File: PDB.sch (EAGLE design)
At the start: 84 parts

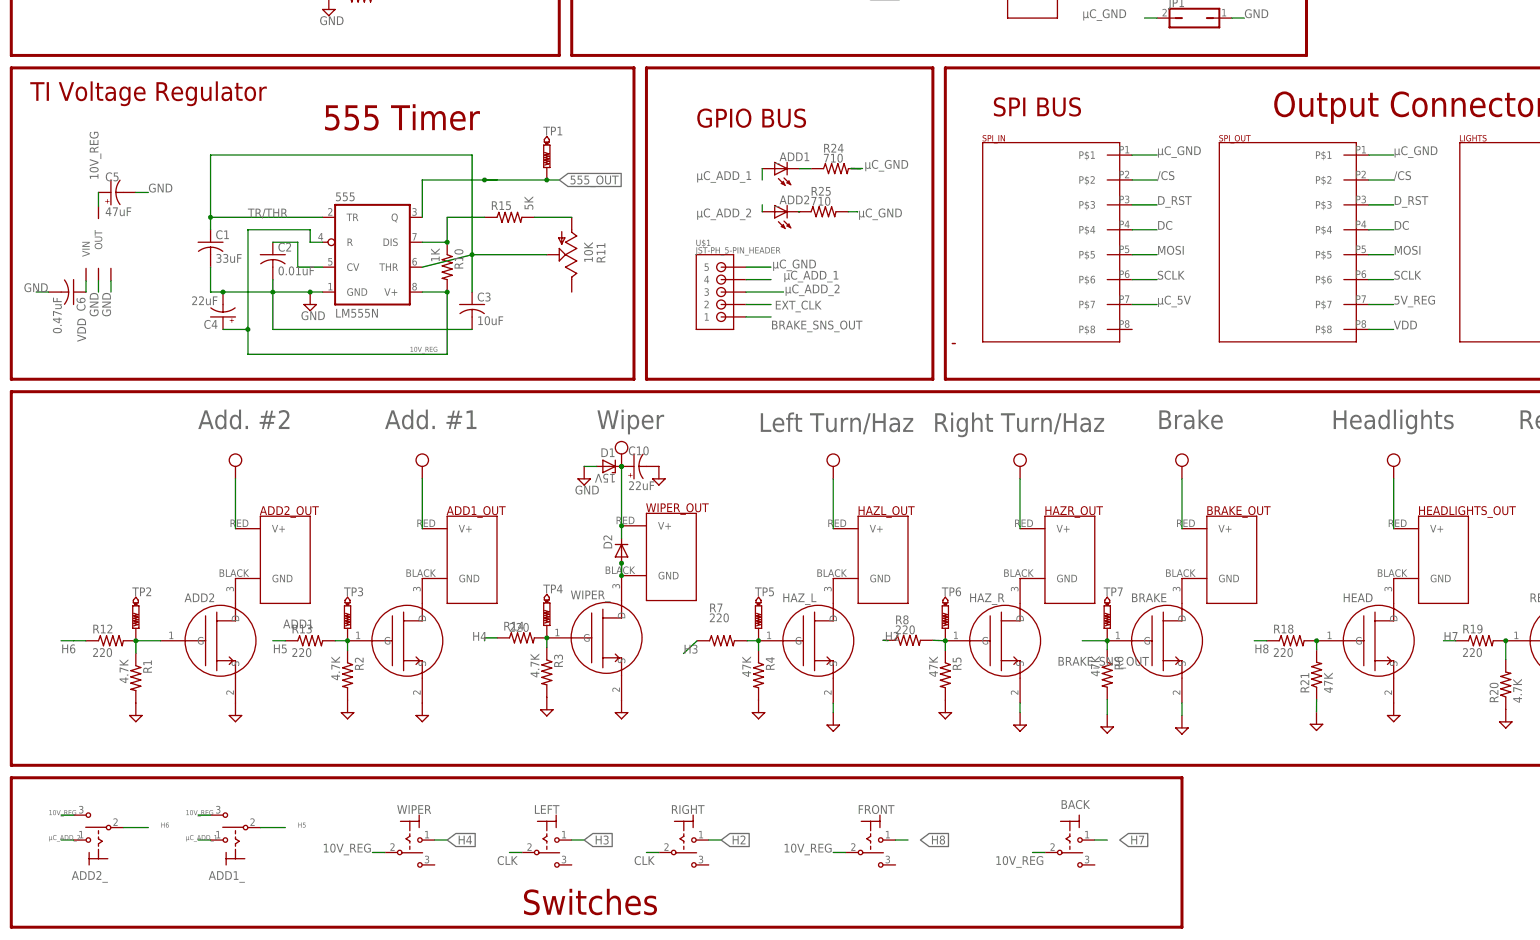
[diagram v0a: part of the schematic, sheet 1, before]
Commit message: Deleted SPI, ADD2
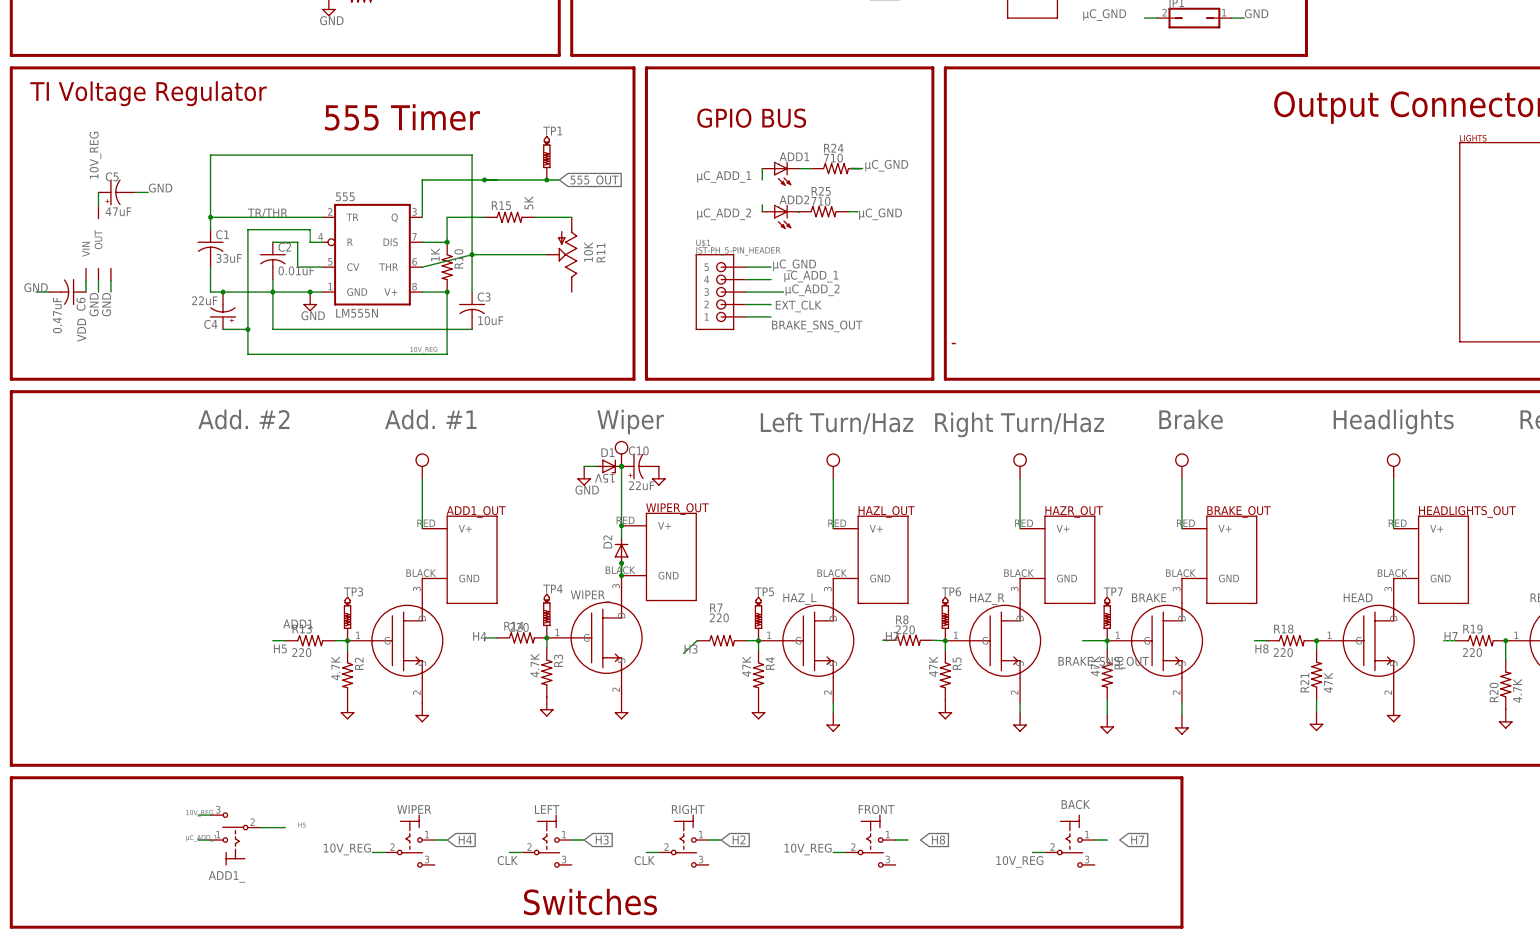
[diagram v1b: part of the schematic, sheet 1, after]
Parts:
- removed ADD2: NCV8405ADPAK-3PIN, master_library:NCV8405ADPAK-3PIN
- removed ADD2_: (no value), switch:M9040P
- removed ADD2_OUT: POWERPOLE_POWER25A_HORIZONTAL_G2, powerpoles:POWERPOLE_POWER25A_HORIZONTAL_G2
- removed R1: 4.7K, rcl:R-US_R0805
- removed R12: 220, rcl:R-US_R0805
- removed SPI_IN, SPI_OUT: 8-PIN-MOLEX-RA-FEMALE, master_library:8-PIN-MOLEX-RA-FEMALE
- removed TP2: PTR1B2,54, testpad:PTR1B2,54
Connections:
- removed net /CS: SPI_IN.P$2, SPI_OUT.P$2
- removed net DC: SPI_IN.P$4, SPI_OUT.P$4
- removed net D_RST: SPI_IN.P$3, SPI_OUT.P$3
- removed net H6: ADD2_.P, R12.1
- removed net MOSI: SPI_IN.P$5, SPI_OUT.P$5
- removed net N$7: ADD2.G, R1.1, R12.2, TP2.TP
- removed net N$8: ADD2.D, ADD2_OUT.GND
- removed net SCLK: SPI_IN.P$6, SPI_OUT.P$6
- removed net µC_5V: SPI_IN.P$7
- net 10V_REG: no longer ADD2_.S
- net 5V_REG: no longer SPI_OUT.P$7
- net GND: no longer ADD2.S, R1.2
- net VDD: no longer ADD2_OUT.V+, SPI_OUT.P$8
- net µC_ADD_2: no longer ADD2_.O
- net µC_GND: no longer SPI_IN.P$1, SPI_OUT.P$1
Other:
- note removed: "SPI BUS"

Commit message: Changed GND to VDD for connector
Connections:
- net GND: no longer LIGHTS.P$6, LIGHTS.P$7, LIGHTS.P$8
- net VDD: now also LIGHTS.P$6, LIGHTS.P$7, LIGHTS.P$8; no longer BRAKE_OUT.V+, REARLIGHTS_OUT.V+
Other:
- note removed: "Add. #2"
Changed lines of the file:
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@@
 <part name="BRAKE" library="master_library" deviceset="NCV8405A" device="DPAK-3PIN" package3d_urn="urn:adsk.eagle:package:8893803/1"/>
 <part name="BRAKE_OUT" library="powerpoles" deviceset="POWERPOLE_POWER" device="25A_HORIZONTAL_G2" value="POWERPOLE_POWER25A_HORIZONTAL_G2"/>
-<part name="SUPPLY35" library="supply2" library_urn="urn:adsk.eagle:library:372" deviceset="VDD" device=""/>
 <part name="SUPPLY36" library="supply2" library_urn="urn:adsk.eagle:library:372" deviceset="GND" device=""/>
 <part name="HEAD" library="master_library" deviceset="NCV8405A" device="DPAK-3PIN" package3d_urn="urn:adsk.eagle:package:8893803/1"/>
@@
 <part name="REAR" library="master_library" deviceset="NCV8405A" device="DPAK-3PIN" package3d_urn="urn:adsk.eagle:package:8893803/1"/>
 <part name="REARLIGHTS_OUT" library="powerpoles" deviceset="POWERPOLE_POWER" device="25A_HORIZONTAL_G2" value="POWERPOLE_POWER25A_HORIZONTAL_G2"/>
-<part name="SUPPLY3" library="supply2" library_urn="urn:adsk.eagle:library:372" deviceset="VDD" device=""/>
 <part name="SUPPLY4" library="supply2" library_urn="urn:adsk.eagle:library:372" deviceset="GND" device=""/>
 <part name="R2" library="rcl" library_urn="urn:adsk.eagle:library:334" deviceset="R-US_" device="R0805" package3d_urn="urn:adsk.eagle:package:23553/2" value="4.7K"/>
@@
 <wire x1="-104.14" y1="81.28" x2="22.86" y2="81.28" width="0.6096" layer="94"/>
 <wire x1="22.86" y1="81.28" x2="22.86" y2="144.78" width="0.6096" layer="94"/>
-<text x="-66.04" y="71.12" size="3.81" layer="95">Add. #2 </text>
 <text x="-27.94" y="71.12" size="3.81" layer="95">Add. #1</text>
 <text x="15.24" y="71.12" size="3.81" layer="95">Wiper</text>
@@
 <attribute name="NAME" x="139.573" y="53.594" size="1.778" layer="94" rot="SR0"/>
 </instance>
-<instance part="SUPPLY35" gate="G$1" x="134.62" y="63.5" smashed="yes"/>
 <instance part="SUPPLY36" gate="GND" x="134.62" y="10.16" smashed="yes"/>
 <instance part="HEAD" gate="G$1" x="162.56" y="27.94" smashed="yes">
@@
 <attribute name="NAME" x="220.853" y="53.594" size="1.778" layer="94" rot="SR0"/>
 </instance>
-<instance part="SUPPLY3" gate="G$1" x="215.9" y="63.5" smashed="yes"/>
 <instance part="SUPPLY4" gate="GND" x="215.9" y="12.7" smashed="yes"/>
 <instance part="R2" gate="G$1" x="-35.56" y="20.905" smashed="yes" rot="R270">
@@
 </segment>
 <segment>
-<pinref part="SUPPLY35" gate="G$1" pin="VDD"/>
-<pinref part="BRAKE_OUT" gate="G$1" pin="V+"/>
-<wire x1="134.62" y1="50.8" x2="134.62" y2="60.96" width="0.1524" layer="91"/>
-</segment>
-<segment>
 <pinref part="SUPPLY1" gate="G$1" pin="VDD"/>
 <pinref part="HEADLIGHTS_OUT" gate="G$1" pin="V+"/>
@@
 </segment>
 <segment>
-<pinref part="SUPPLY3" gate="G$1" pin="VDD"/>
-<pinref part="REARLIGHTS_OUT" gate="G$1" pin="V+"/>
-<wire x1="215.9" y1="60.96" x2="215.9" y2="50.8" width="0.1524" layer="91"/>
-</segment>
-<segment>
 <pinref part="U$2" gate="G$1" pin="1"/>
 <wire x1="77.216" y1="168.264" x2="71.12" y2="168.264" width="0.1524" layer="91"/>
@@
 <wire x1="81.28" y1="175.26" x2="78.74" y2="175.26" width="0.1524" layer="91"/>
 <label x="73.66" y="175.26" size="1.778" layer="95"/>
+</segment>
+<segment>
+<pinref part="LIGHTS" gate="G$1" pin="P$6"/>
+<wire x1="221.765" y1="101.6" x2="223.52" y2="101.6" width="0.1524" layer="91"/>
+<wire x1="224.79" y1="101.6" x2="223.52" y2="101.6" width="0.1524" layer="91"/>
+<label x="224.536" y="101.854" size="1.778" layer="95"/>
+</segment>
+<segment>
+<pinref part="LIGHTS" gate="G$1" pin="P$7"/>
+<wire x1="221.765" y1="96.52" x2="223.52" y2="96.52" width="0.1524" layer="91"/>
+<wire x1="224.536" y1="96.52" x2="223.52" y2="96.52" width="0.1524" layer="91"/>
+<label x="224.79" y="96.52" size="1.778" layer="95"/>
+</segment>
+<segment>
+<pinref part="LIGHTS" gate="G$1" pin="P$8"/>
+<wire x1="221.765" y1="91.44" x2="225.044" y2="91.44" width="0.1524" layer="91"/>
+<label x="225.044" y="91.694" size="1.778" layer="95"/>
 </segment>
 </net>
@@
 </segment>
 <segment>
-<pinref part="LIGHTS" gate="G$1" pin="P$8"/>
-<wire x1="221.765" y1="91.44" x2="224.305" y2="91.44" width="0.1524" layer="91"/>
-<label x="224.305" y="91.44" size="1.778" layer="95"/>
-</segment>
-<segment>
 <pinref part="SUPPLY17" gate="GND" pin="GND"/>
 <pinref part="R17" gate="G$1" pin="2"/>
@@
 </segment>
 <segment>
-<pinref part="LIGHTS" gate="G$1" pin="P$7"/>
-<wire x1="221.765" y1="96.52" x2="223.52" y2="96.52" width="0.1524" layer="91"/>
-<label x="223.52" y="96.52" size="1.778" layer="95"/>
-</segment>
-<segment>
-<pinref part="LIGHTS" gate="G$1" pin="P$6"/>
-<wire x1="221.765" y1="101.6" x2="223.52" y2="101.6" width="0.1524" layer="91"/>
-<label x="223.52" y="101.6" size="1.778" layer="95"/>
-</segment>
-<segment>

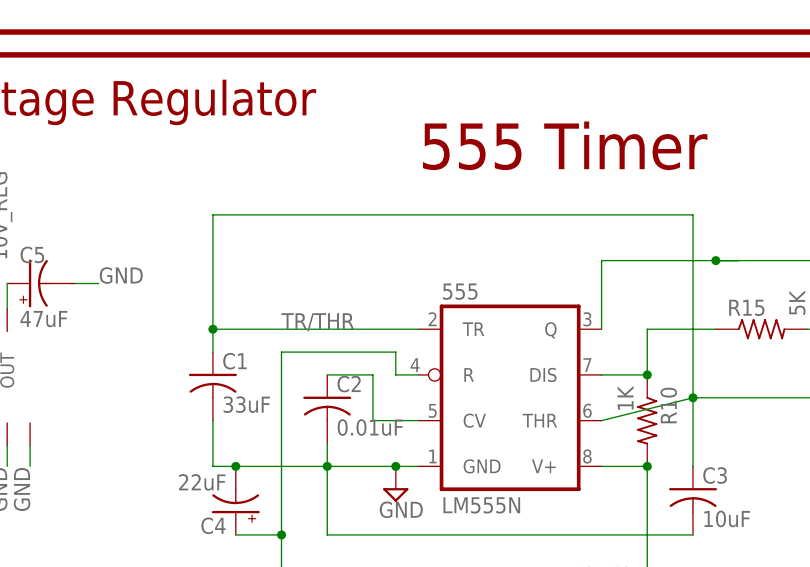
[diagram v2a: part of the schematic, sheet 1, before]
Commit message: Disconnected 555-timer from the jumper
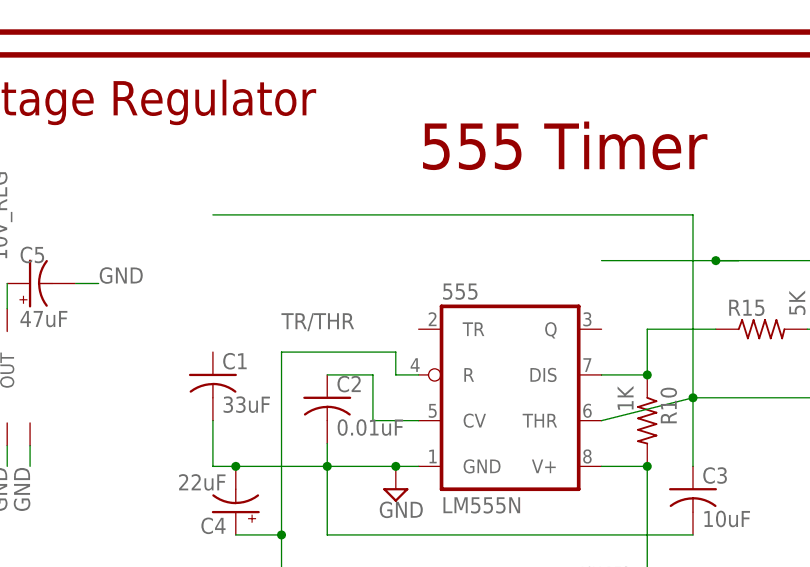
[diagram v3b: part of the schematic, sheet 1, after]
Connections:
- net 555_OUT: no longer 555.Q
- net TR/THR: no longer 555.TR, C1.1
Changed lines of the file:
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@@
 <junction x="5.08" y="121.92"/>
 <wire x1="5.16475625" y1="121.92" x2="5.08" y2="121.92" width="0.1524" layer="91"/>
-<wire x1="-20.32" y1="114.3" x2="-20.32" y2="121.92" width="0.1524" layer="91"/>
 <wire x1="-20.32" y1="121.92" x2="-7.62" y2="121.92" width="0.1524" layer="91"/>
-<pinref part="555" gate="A" pin="Q"/>
 <wire x1="-7.62" y1="121.92" x2="-5.08" y2="121.92" width="0.1524" layer="91"/>
 <wire x1="5.08" y1="121.92" x2="-7.62" y2="121.92" width="0.1524" layer="91"/>
@@
 <net name="TR/THR" class="0">
 <segment>
-<wire x1="-40.64" y1="114.3" x2="-63.5" y2="114.3" width="0.1524" layer="91"/>
-<pinref part="C1" gate="G$1" pin="1"/>
-<wire x1="-63.5" y1="114.3" x2="-63.5" y2="111.76" width="0.1524" layer="91"/>
-<wire x1="-63.5" y1="114.3" x2="-63.5" y2="127" width="0.1524" layer="91"/>
-<junction x="-63.5" y="114.3"/>
 <wire x1="-63.5" y1="127" x2="-10.16" y2="127" width="0.1524" layer="91"/>
 <wire x1="-10.16" y1="127" x2="-10.16" y2="106.68" width="0.1524" layer="91"/>
@@
 <pinref part="R11" gate="G$1" pin="S"/>
 <wire x1="5.08" y1="106.68" x2="-10.16" y2="106.68" width="0.1524" layer="91"/>
-<pinref part="555" gate="A" pin="TR"/>
 <pinref part="555" gate="A" pin="THR"/>
 </segment>

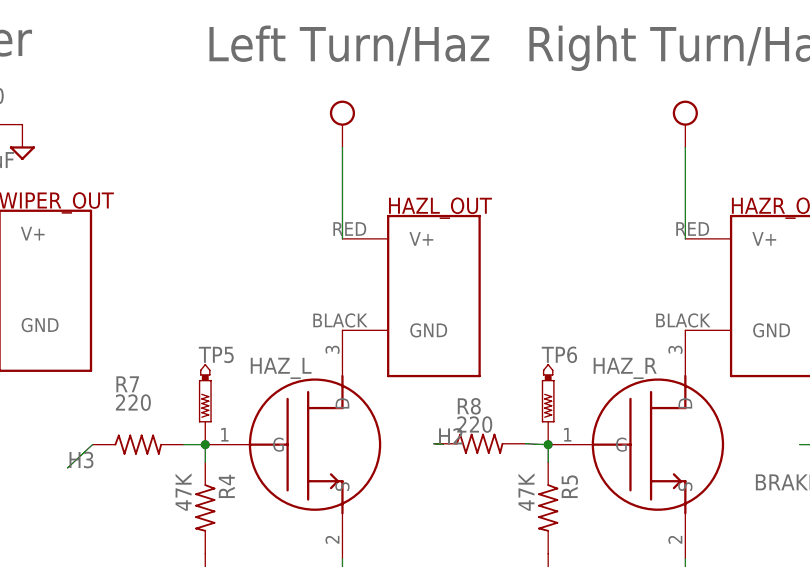
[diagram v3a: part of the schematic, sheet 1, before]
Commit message: Deleted Anderson connector for left and right light
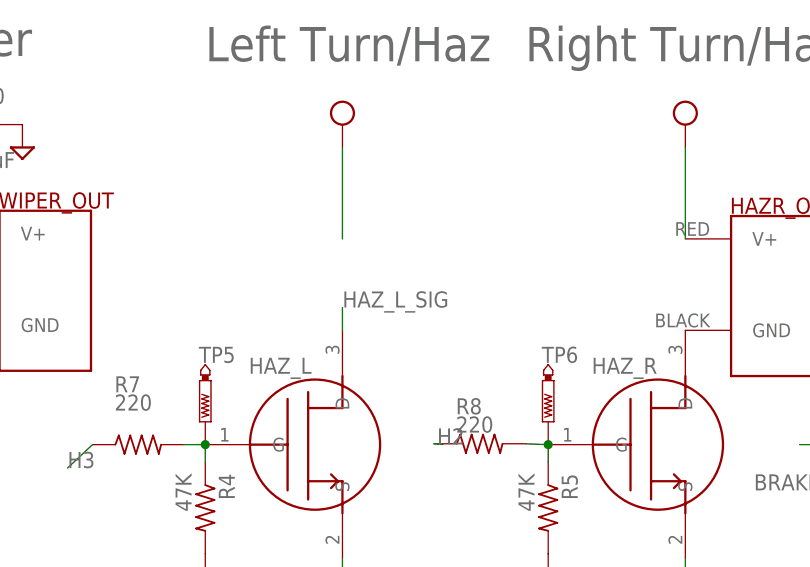
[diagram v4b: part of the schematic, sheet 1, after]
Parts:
- removed HAZL_OUT: POWERPOLE_POWER25A_HORIZONTAL_G2, powerpoles:POWERPOLE_POWER25A_HORIZONTAL_G2
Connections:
- net HAZ_L_SIG: no longer HAZL_OUT.GND
- net VDD: no longer HAZL_OUT.V+
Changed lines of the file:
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@@
 <part name="SUPPLY30" library="supply2" library_urn="urn:adsk.eagle:library:372" deviceset="GND" device=""/>
 <part name="HAZ_L" library="master_library" deviceset="NCV8405A" device="DPAK-3PIN" package3d_urn="urn:adsk.eagle:package:8893803/1"/>
-<part name="HAZL_OUT" library="powerpoles" deviceset="POWERPOLE_POWER" device="25A_HORIZONTAL_G2" value="POWERPOLE_POWER25A_HORIZONTAL_G2"/>
 <part name="SUPPLY31" library="supply2" library_urn="urn:adsk.eagle:library:372" deviceset="VDD" device=""/>
 <part name="HAZ_R" library="master_library" deviceset="NCV8405A" device="DPAK-3PIN" package3d_urn="urn:adsk.eagle:package:8893803/1"/>
@@
 <attribute name="NAME" x="53.096034375" y="35.814" size="1.778" layer="95" font="vector" rot="SR0"/>
 </instance>
-<instance part="HAZL_OUT" gate="G$1" x="73.66" y="45.72" smashed="yes">
-<attribute name="NAME" x="68.453" y="53.594" size="1.778" layer="94" rot="SR0"/>
-</instance>
 <instance part="SUPPLY31" gate="G$1" x="63.5" y="63.5" smashed="yes"/>
 <instance part="HAZ_R" gate="G$1" x="86.36" y="27.94" smashed="yes">
@@
 <segment>
 <pinref part="SUPPLY31" gate="G$1" pin="VDD"/>
-<pinref part="HAZL_OUT" gate="G$1" pin="V+"/>
 <wire x1="63.5" y1="50.8" x2="63.5" y2="60.96" width="0.1524" layer="91"/>
 </segment>
@@
 <net name="HAZ_L_SIG" class="0">
 <segment>
-<pinref part="HAZ_L" gate="G$1" pin="D"/>
-<pinref part="HAZL_OUT" gate="G$1" pin="GND"/>
-</segment>
-<segment>
 <pinref part="LIGHTS" gate="G$1" pin="P$2"/>
 <wire x1="221.765" y1="121.92" x2="224.305" y2="121.92" width="0.1524" layer="91"/>
 <label x="224.305" y="121.92" size="1.778" layer="95"/>
 </segment>
+<segment>
+<pinref part="HAZ_L" gate="G$1" pin="D"/>
+<wire x1="63.5" y1="40.64" x2="63.5" y2="43.18" width="0.1524" layer="91"/>
+<label x="63.5" y="43.18" size="1.778" layer="95"/>
+</segment>
 </net>
